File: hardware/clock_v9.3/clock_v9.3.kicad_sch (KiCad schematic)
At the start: 68 parts, among them J4 USB_C_Receptacle, J8 Conn_01x02, U11 AMS1117-3.3, U12 BA50DD0WHFP-TR, U14 CH340C, U15 USBLC6-2P6, U21 74LVC1G86, U22 74LVC1G00, U23 TPS63060, U9 L78L05_SOT89

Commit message: cleanup existing schematic
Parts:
- removed C30, C31, C32, C36, C38: 100n, Capacitor_SMD:C_0402_1005Metric, symbol Device:C_Small
- removed H1, H2, H3, H4: M2, MountingHole:MountingHole_2.2mm_M2, symbol Mechanical:MountingHole
- removed U21: 74LVC1G86, Package_TO_SOT_SMD:SOT-23-5, symbol 74xGxx:74LVC1G86
- removed U22: 74LVC1G00, Package_TO_SOT_SMD:SOT-23-5, symbol 74xGxx:74LVC1G00
- added C1: 100n, Capacitor_SMD:C_0402_1005Metric, symbol Device:C_Small
- added JP10, JP11, JP12, JP3: SolderJumper_2_Bridged, Jumper:SolderJumper-2_P1.3mm_Bridged2Bar_RoundedPad1.0x1.5mm, symbol Jumper:SolderJumper_2_Bridged
- added TP1, TP10, TP11, TP12, TP13, TP14, TP15, TP5, TP6, TP7, TP8, TP9: ~, TestPoint:TestPoint_THTPad_D1.5mm_Drill0.7mm, symbol Connector:TestPoint
- added U1, U2, U3: SN74LVC1G14DBV, Package_TO_SOT_SMD:SOT-23-5, symbol 74xGxx:SN74LVC1G14DBV
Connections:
- net +3.3V: now also C1.1, JP11.1 (A), TP11.1, U1.5 (VCC), U2.5 (VCC), U3.5 (VCC); no longer FB1.1
- net +3.3VA: now also TP13.1
- net +5V: now also TP15.1; no longer C42.1
- net +5VA: now also TP7.1
- net +6V: now also JP10.1 (A), JP12.2 (B), JP3.1 (A); no longer C33.2, C39.2, C44.1, JP5.2 (B), U11.3 (VI), U12.2 (VCC), U9.3 (IN)
- net BOOT0: now also TP9.1
- net GND: now also C1.2, U1.3 (GND), U2.3 (GND), U3.3 (GND)
- net NRST: now also TP10.1
- net USB_DTR: now also TP1.1, U1.2
- net USB_RTS: now also TP5.1, U2.2
- net at JP4.1 (A), U12.4 (OUT): now also C42.1
- net at R41.1: now also U2.4
- net at R42.2: now also U3.4
- net FVIN renamed VIN1
- net FVOUT renamed VOUT1
- new net: U1.4, U3.2
- new net VIN2: C39.2, JP10.2 (B), TP8.1, U11.3 (VI)
- new net VIN3: C33.2, JP3.2 (B), TP6.1, U9.3 (IN)
- new net VIN4: C44.1, JP12.1 (A), JP5.2 (B), TP14.1, U12.2 (VCC)
- new net VIN5: FB1.1, JP11.2 (B), TP12.1
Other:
- note removed: "Mounting Holes"
- moved on the sheet: C27, C33, C34, C37, C39, C41, C42, C43, C44, C50, C58, C59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

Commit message: start new switch regulator layout
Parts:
- added C2, C3: 10uF, Capacitor_SMD:C_0603_1608Metric, symbol Device:C_Small
- added C4, C5, C6: 22uF, Capacitor_SMD:C_0805_2012Metric, symbol Device:C_Small
- added C7: 10pF, Capacitor_SMD:C_0603_1608Metric, symbol Device:C_Small
- added D1: B330, Diode_SMD:D_SMC, symbol Diode:B330
- added L1: 10uH, Inductor_SMD:L_Coilcraft_XAL4020-XXX, symbol Device:L
- added R1: 1K0, Resistor_SMD:R_0603_1608Metric, symbol Device:R_Small_US
- added R2: 12K, Resistor_SMD:R_0603_1608Metric, symbol Device:R_Small_US
- added R3: 120K, Resistor_SMD:R_0603_1608Metric, symbol Device:R_Small_US
- added U4: LM2731XMF, Package_TO_SOT_SMD:SOT-23-5, symbol Regulator_Switching:LM2731XMF
- R31: JLCPCB Part # (none) -> C25808
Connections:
- net GND: now also C2.2, C3.2, C4.2, C5.2, C6.2, R2.2, U4.2 (GND)
- new net: C7.2, R2.1, R3.2, U4.3 (FB)
- new net: R1.2, U4.4 (EN)
- new net VIN6: C2.1, C3.1, L1.2, R1.1, U4.5 (VIN)
- new net VOUT6: C4.1, C5.1, C6.1, C7.1, D1.1 (K), R3.1
- new net VSW6: D1.2 (A), L1.1, U4.1 (SW)

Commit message: start 2nd supply
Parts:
- added C10, C12, C13: 22uF, Capacitor_SMD:C_0805_2012Metric, symbol Device:C_Small
- added C11: 470pF, Capacitor_SMD:C_0603_1608Metric, symbol Device:C_Small
- added C8, C9: 10uF, Capacitor_SMD:C_0603_1608Metric, symbol Device:C_Small
- added D2: B330, Diode_SMD:D_SMC, symbol Diode:B330
- added JP13, JP14: SolderJumper_2_Bridged, Jumper:SolderJumper-2_P1.3mm_Bridged2Bar_RoundedPad1.0x1.5mm, symbol Jumper:SolderJumper_2_Bridged
- added L2: 10uH, Inductor_SMD:L_Coilcraft_XAL4020-XXX, symbol Device:L
- added R4: 1K0, Resistor_SMD:R_0603_1608Metric, symbol Device:R_Small_US
- added R5: 10K, Resistor_SMD:R_0603_1608Metric, symbol Device:R_Small_US
- added R6: 39K, Resistor_SMD:R_0603_1608Metric, symbol Device:R_Small_US
- added TP16, TP17, TP18, TP19, TP20, TP21, TP22, TP23: ~, TestPoint:TestPoint_THTPad_D1.5mm_Drill0.7mm, symbol Connector:TestPoint
- added U5: LM2731XMF, Package_TO_SOT_SMD:SOT-23-5, symbol Regulator_Switching:LM2731XMF
- C7: value 10pF -> 470pF; JLCPCB Part # C1634 -> C1620
- R2: value 12K -> 10K; JLCPCB Part # C22790 -> C25804
- R3: value 120K -> 39K; JLCPCB Part # C25808 -> C23153
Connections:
- net GND: now also C10.2, C12.2, C13.2, C8.2, C9.2, R5.2, U5.2 (GND)
- net VBUS: now also JP13.1 (A), JP14.1 (A)
- net VIN6: now also JP13.2 (B), TP16.1
- net VOUT6: now also TP19.1
- net VSW6: now also TP17.1
- net at C7.2, R2.1, R3.2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: now also TP18.1
- new net: R4.2, U5.4 (EN)
- new net: C11.2, R5.1, R6.2, TP22.1, U5.3 (FB)
- new net VIN7: C8.1, C9.1, JP14.2 (B), L2.2, R4.1, TP20.1, U5.5 (VIN)
- new net VOUT7: C10.1, C11.1, C12.1, C13.1, D2.1 (K), R6.1, TP23.1
- new net VSW7: D2.2 (A), L2.1, TP21.1, U5.1 (SW)
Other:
- note added: "FB voltage should by 1.230V With resistor to GND about 10K Want ratio about 3.878 39K and 10K gives 6.03 V"
- moved on the sheet: C2, C3, C4, C5, C6, C7, D1, L1, R1, R2, R3, U4

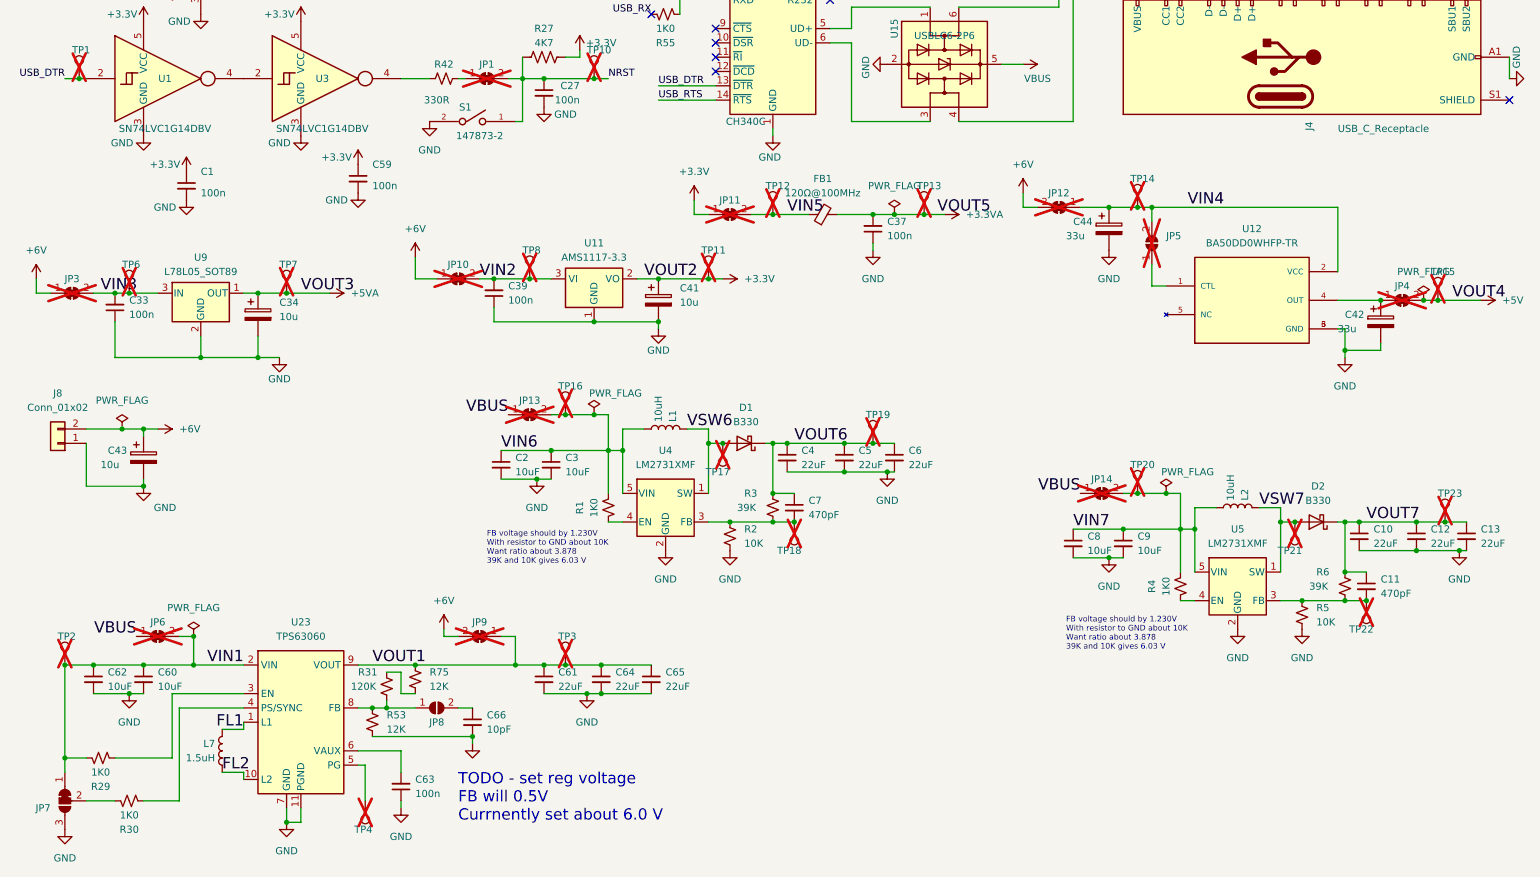
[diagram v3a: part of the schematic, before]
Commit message: update board for HW 9.3
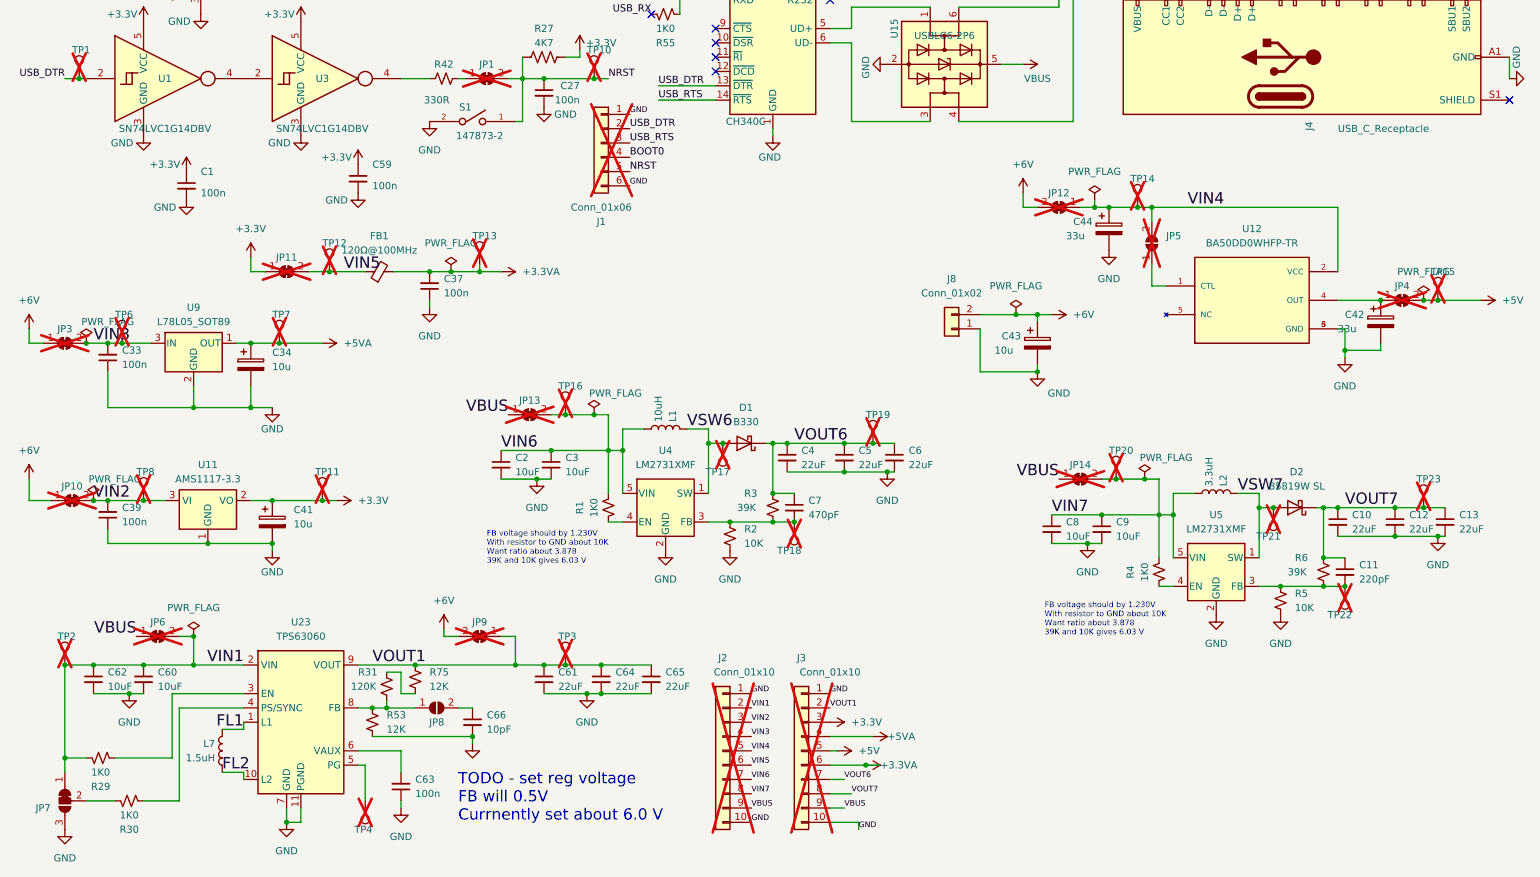
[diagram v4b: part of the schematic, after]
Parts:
- removed D2: B330, Diode_SMD:D_SMC, symbol Diode:B330
- added D2: B5819W SL, Diode_SMD:D_SOD-123, symbol Diode:MBR0520
- added J1: Conn_01x06, Connector_PinHeader_2.54mm:PinHeader_1x06_P2.54mm_Vertical, symbol Connector_Generic:Conn_01x06
- added J2, J3: Conn_01x10, Connector_PinHeader_2.54mm:PinHeader_1x10_P2.54mm_Vertical, symbol Connector_Generic:Conn_01x10
- C11: value 470pF -> 220pF; JLCPCB Part # C1620 -> C1603
- L1: footprint Inductor_SMD:L_Coilcraft_XAL4020-XXX -> Inductor_SMD:L_Coilcraft_XAL4040-XXX
- L2: value 10uH -> 3.3uH; JLCPCB Part # C5144883 -> C19191633; MPN XAL4040-103MEC -> XFL4020-332MEC
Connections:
- net +3.3V: now also J3.3 (Pin_3)
- net +3.3VA: now also J3.6 (Pin_6)
- net +5V: now also J3.5 (Pin_5)
- net +5VA: now also J3.4 (Pin_4)
- net BOOT0: now also J1.4 (Pin_4)
- net GND: now also J1.1 (Pin_1), J1.6 (Pin_6), J2.1 (Pin_1), J2.10 (Pin_10), J3.1 (Pin_1), J3.10 (Pin_10)
- net NRST: now also J1.5 (Pin_5)
- net USB_DTR: now also J1.2 (Pin_2)
- net USB_RTS: now also J1.3 (Pin_3)
- net VBUS: now also J2.9 (Pin_9), J3.9 (Pin_9)
- net VIN1: now also J2.2 (Pin_2)
- net VIN2: now also J2.3 (Pin_3)
- net VIN3: now also J2.4 (Pin_4)
- net VIN4: now also J2.5 (Pin_5)
- net VIN5: now also J2.6 (Pin_6)
- net VIN6: now also J2.7 (Pin_7)
- net VIN7: now also J2.8 (Pin_8)
- net VOUT1: now also J3.2 (Pin_2)
- net VOUT6: now also J3.7 (Pin_7)
- net VOUT7: now also D2.1 (K), J3.8 (Pin_8)
- net VSW7: now also D2.2 (A)
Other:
- moved on the sheet: C10, C11, C12, C13, C33, C34, C37, C39, C41, C43, C8, C9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

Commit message: clean up
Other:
- note added: "FB will 0.5V Currnently set about 6.0 V with 12k and 132k"
- note removed: "TODO - set reg voltage FB will 0.5V Currnently set about 6.0 V"
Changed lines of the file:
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@@
     (effects (font (size 1 1)) (justify left bottom))
   )
-  (text "TODO - set reg voltage\nFB will 0.5V \nCurrnently set about 6.0 V "
-    (at 93.98 187.96 0)
-    (effects (font (size 2 2)) (justify left bottom))
+  (text "FB will 0.5V \nCurrnently set about 6.0 V \nwith 12k and 132k "
+    (at 93.98 184.15 0)
+    (effects (font (size 1 1)) (justify left bottom))
   )
   (text "FB voltage should by 1.230V \nWith resistor to GND about 10K \nWant ratio about 3.878\n39K and 10K gives 6.03 V\n"
@@
   )
   (label "VOUT6" (at 153.67 120.65 0) (fields_autoplaced)
-    (effects (font (size 2 2)) (justify left bottom))
+    (effects (font (size 1 1)) (justify left bottom))
   )
   (label "GND" (at 146.05 187.96 0) (fields_autoplaced)
@@
   )
   (label "VSW7" (at 232.41 129.54 0) (fields_autoplaced)
-    (effects (font (size 2 2)) (justify left bottom))
+    (effects (font (size 1 1)) (justify left bottom))
   )
   (label "BOOT0" (at 114.3 34.29 0) (fields_autoplaced)
@@
   )
   (label "VSW6" (at 134.62 118.11 0) (fields_autoplaced)
-    (effects (font (size 2 2)) (justify left bottom))
+    (effects (font (size 1 1)) (justify left bottom))
   )
   (label "NRST" (at 120.65 55.88 0) (fields_autoplaced)
@@
   )
   (label "VIN7" (at 199.39 133.35 0) (fields_autoplaced)
-    (effects (font (size 2 2)) (justify left bottom))
+    (effects (font (size 1 1)) (justify left bottom))
   )
   (label "VIN3" (at 146.05 172.72 0) (fields_autoplaced)
@@
   )
   (label "VBUS" (at 200.66 127 180) (fields_autoplaced)
-    (effects (font (size 2 2)) (justify right bottom))
+    (effects (font (size 1 1)) (justify right bottom))
   )
   (label "VIN5" (at 146.05 177.8 0) (fields_autoplaced)
@@
   )
   (label "VBUS" (at 102.87 115.57 180) (fields_autoplaced)
-    (effects (font (size 2 2)) (justify right bottom))
+    (effects (font (size 1 1)) (justify right bottom))
   )
   (label "VIN1" (at 55.88 160.02 180) (fields_autoplaced)

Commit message: add yet antoehr power connector
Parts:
- added J5: DC-005-20A, Connector_BarrelJack:BarrelJack_Horizontal, symbol Connector:Barrel_Jack_Switch_Pin3Ring
- added TP24, TP25, TP26: ~, TestPoint:TestPoint_THTPad_D1.5mm_Drill0.7mm, symbol Connector:TestPoint
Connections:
- new net: J5.1, TP24.1
- new net: J5.2, TP26.1
- new net: J5.3, TP25.1
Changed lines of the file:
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@@
     (stroke (width 0) (type default))
   )
+  (wire (pts (xy 149.86 90.17) (xy 156.21 90.17))
+    (stroke (width 0) (type default))
+  )
   (wire (pts (xy 26.67 55.88) (xy 27.94 55.88))
     (stroke (width 0) (type default))
@@
     (stroke (width 0) (type default))
   )
+  (wire (pts (xy 149.86 92.71) (xy 153.67 92.71))
+    (stroke (width 0) (type default))
+  )
   (wire (pts (xy 66.04 185.42) (xy 66.04 187.96))
     (stroke (width 0) (type default))
@@
     (stroke (width 0) (type default))
   )
+  (wire (pts (xy 153.67 87.63) (xy 153.67 86.36))
+    (stroke (width 0) (type default))
+  )
   (wire (pts (xy 83.82 55.88) (xy 88.9 55.88))
     (stroke (width 0) (type default))
   )
+  (wire (pts (xy 149.86 87.63) (xy 153.67 87.63))
+    (stroke (width 0) (type default))
+  )
   (wire (pts (xy 52.07 179.07) (xy 55.88 179.07))
     (stroke (width 0) (type default))
@@
     (stroke (width 0) (type default))
   )
+  (wire (pts (xy 153.67 92.71) (xy 153.67 93.98))
+    (stroke (width 0) (type default))
+  )
   (wire (pts (xy 224.79 34.29) (xy 245.11 34.29))
     (stroke (width 0) (type default))
@@
     )
   )
+  (symbol (lib_id "Connector:Barrel_Jack_Switch_Pin3Ring") (at 142.24 90.17 0) (unit 1)
+    (in_bom yes) (on_board yes) (dnp no)
+    (property "Reference" "J5" (at 142.24 82.55 0)
+      (effects (font (size 1.27 1.27)))
+    )
+    (property "Value" "DC-005-20A" (at 142.24 85.09 0)
+      (effects (font (size 1.27 1.27)))
+    )
+    (property "Footprint" "Connector_BarrelJack:BarrelJack_Horizontal" (at 143.51 91.186 0)
+      (effects (font (size 1.27 1.27)) hide)
+    )
+    (property "Datasheet" "~" (at 143.51 91.186 0)
+      (effects (font (size 1.27 1.27)) hide)
+    )
+    (property "JLCPCB Part #" "C136744" (at 142.24 90.17 0)
+      (effects (font (size 1.27 1.27)) hide)
+    )
+    (property "MANUFACTURER" "Korean Hroparts Elec" (at 142.24 90.17 0)
+      (effects (font (size 1.27 1.27)) hide)
+    )
+    (property "JLCPCB Position Offset" "" (at 142.24 90.17 0)
+      (effects (font (size 1.27 1.27)) hide)
+    )
+    (pin "1")
+    (pin "2")
+    (pin "3")
+    (instances
+      (project "clock_v9.3"
+        (path "/bd4d3b9a-07c1-4a53-9c94-2893f3e869d4"
+          (reference "J5") (unit 1)
+        )
+      )
+    )
+  )
   (symbol (lib_id "Connector_Generic:Conn_01x10") (at 140.97 175.26 0) (mirror y) (unit 1)
     (in_bom no) (on_board yes) (dnp yes)
@@
     )
   )
+  (symbol (lib_id "Connector:TestPoint") (at 153.67 93.98 180) (unit 1)
+    (in_bom no) (on_board yes) (dnp yes)
+    (property "Reference" "TP25" (at 154.94 99.06 0)
+      (effects (font (size 1.27 1.27)) (justify left))
+    )
+    (property "Value" "~" (at 154.94 100.33 0)
+      (effects (font (size 1.27 1.27)) (justify left))
+    )
+    (property "Footprint" "TestPoint:TestPoint_THTPad_D1.5mm_Drill0.7mm" (at 148.59 93.98 0)
+      (effects (font (size 1.27 1.27)) hide)
+    )
+    (property "Datasheet" "~" (at 148.59 93.98 0)
+      (effects (font (size 1.27 1.27)) hide)
+    )
+    (pin "1")
+    (instances
+      (project "clock_v9.3"
+        (path "/bd4d3b9a-07c1-4a53-9c94-2893f3e869d4"
+          (reference "TP25") (unit 1)
+        )
+      )
+    )
+  )
   (symbol (lib_id "power:GND") (at 170.18 125.73 0) (unit 1)
     (in_bom yes) (on_board yes) (dnp no) (fields_autoplaced)
@@
     )
   )
+  (symbol (lib_id "Connector:TestPoint") (at 156.21 90.17 270) (unit 1)
+    (in_bom no) (on_board yes) (dnp yes)
+    (property "Reference" "TP26" (at 161.29 88.9 0)
+      (effects (font (size 1.27 1.27)) (justify left))
+    )
+    (property "Value" "~" (at 162.56 88.9 0)
+      (effects (font (size 1.27 1.27)) (justify left))
+    )
+    (property "Footprint" "TestPoint:TestPoint_THTPad_D1.5mm_Drill0.7mm" (at 156.21 95.25 0)
+      (effects (font (size 1.27 1.27)) hide)
+    )
+    (property "Datasheet" "~" (at 156.21 95.25 0)
+      (effects (font (size 1.27 1.27)) hide)
+    )
+    (pin "1")
+    (instances
+      (project "clock_v9.3"
+        (path "/bd4d3b9a-07c1-4a53-9c94-2893f3e869d4"
+          (reference "TP26") (unit 1)
+        )
+      )
+    )
+  )
   (symbol (lib_id "Connector:TestPoint") (at 26.67 55.88 0) (unit 1)
     (in_bom no) (on_board yes) (dnp yes)
@@
         )
       )
+    )
+  )
+  (symbol (lib_id "Connector:TestPoint") (at 153.67 86.36 0) (unit 1)
+    (in_bom no) (on_board yes) (dnp yes)
+    (property "Reference" "TP24" (at 152.4 81.28 0)
+      (effects (font (size 1.27 1.27)) (justify left))
+    )
+    (property "Value" "~" (at 152.4 80.01 0)
+      (effects (font (size 1.27 1.27)) (justify left))
+    )
+    (property "Footprint" "TestPoint:TestPoint_THTPad_D1.5mm_Drill0.7mm" (at 158.75 86.36 0)
+      (effects (font (size 1.27 1.27)) hide)
+    )
+    (property "Datasheet" "~" (at 158.75 86.36 0)
+      (effects (font (size 1.27 1.27)) hide)
+    )
+    (pin "1")
+    (instances
+      (project "clock_v9.3"
+        (path "/bd4d3b9a-07c1-4a53-9c94-2893f3e869d4"
+          (reference "TP24") (unit 1)
+        )
+      )

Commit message: send off 9.3 version of power board
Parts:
- J5: JLCPCB Position Offset (none) -> -3.2,-2.3
- U23: JLCPCB Rotation Offset (none) -> 270
- U4, U5: JLCPCB Rotation Offset (none) -> 180
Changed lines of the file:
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@@
       (effects (font (size 1.27 1.27)) hide)
     )
+    (property "JLCPCB Rotation Offset" "270" (at 66.04 170.18 0)
+      (effects (font (size 1.27 1.27)) hide)
+    )
     (pin "1")
     (pin "10")
@@
       (effects (font (size 1.27 1.27)) hide)
     )
-    (property "JLCPCB Position Offset" "" (at 142.24 90.17 0)
+    (property "JLCPCB Position Offset" "-3.2,-2.3" (at 142.24 90.17 0)
       (effects (font (size 1.27 1.27)) hide)
     )
@@
       (effects (font (size 1.27 1.27)) hide)
     )
+    (property "JLCPCB Rotation Offset" "180" (at 130.81 132.08 0)
+      (effects (font (size 1.27 1.27)) hide)
+    )
     (pin "1")
     (pin "2")
@@
       (effects (font (size 1.27 1.27)) hide)
     )
+    (property "JLCPCB Rotation Offset" "180" (at 228.6 143.51 0)
+      (effects (font (size 1.27 1.27)) hide)
+    )
